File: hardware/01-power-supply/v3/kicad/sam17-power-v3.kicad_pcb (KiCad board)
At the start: 2 copper layers, 200 x 150 mm, 114 parts, among them J1 Barrier block 3 pos, J2 Molex KK-254 4 pos, J3 Barrier block 3 pos, J4 Barrier block 2 pos, J5 Faston macho 6.3mm PCB, J6 Molex KK-254 2 pos, J7 Barrier block 2 pos, J8 JST-PH 4 pos, U1 LM2941CT/NOPB, U10 ADS1115IDGSR — ADC 16 bits 4 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, U11 TMP1075DGKR — sensor de tempe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, U12 ISO1541D — aislador I2C bidir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, U2 LM2991T/NOPB, U3 LM7805, U4 LT3045EDD#TRPBF, U5 LT3045EDD#TRPBF, U6 LT3094EDD#PBF, U7 LT3094EDD#PBF, U8 INA226AIDGSR — monitor I/V I2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, U9 INA226AIDGSR — monitor I/V I2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

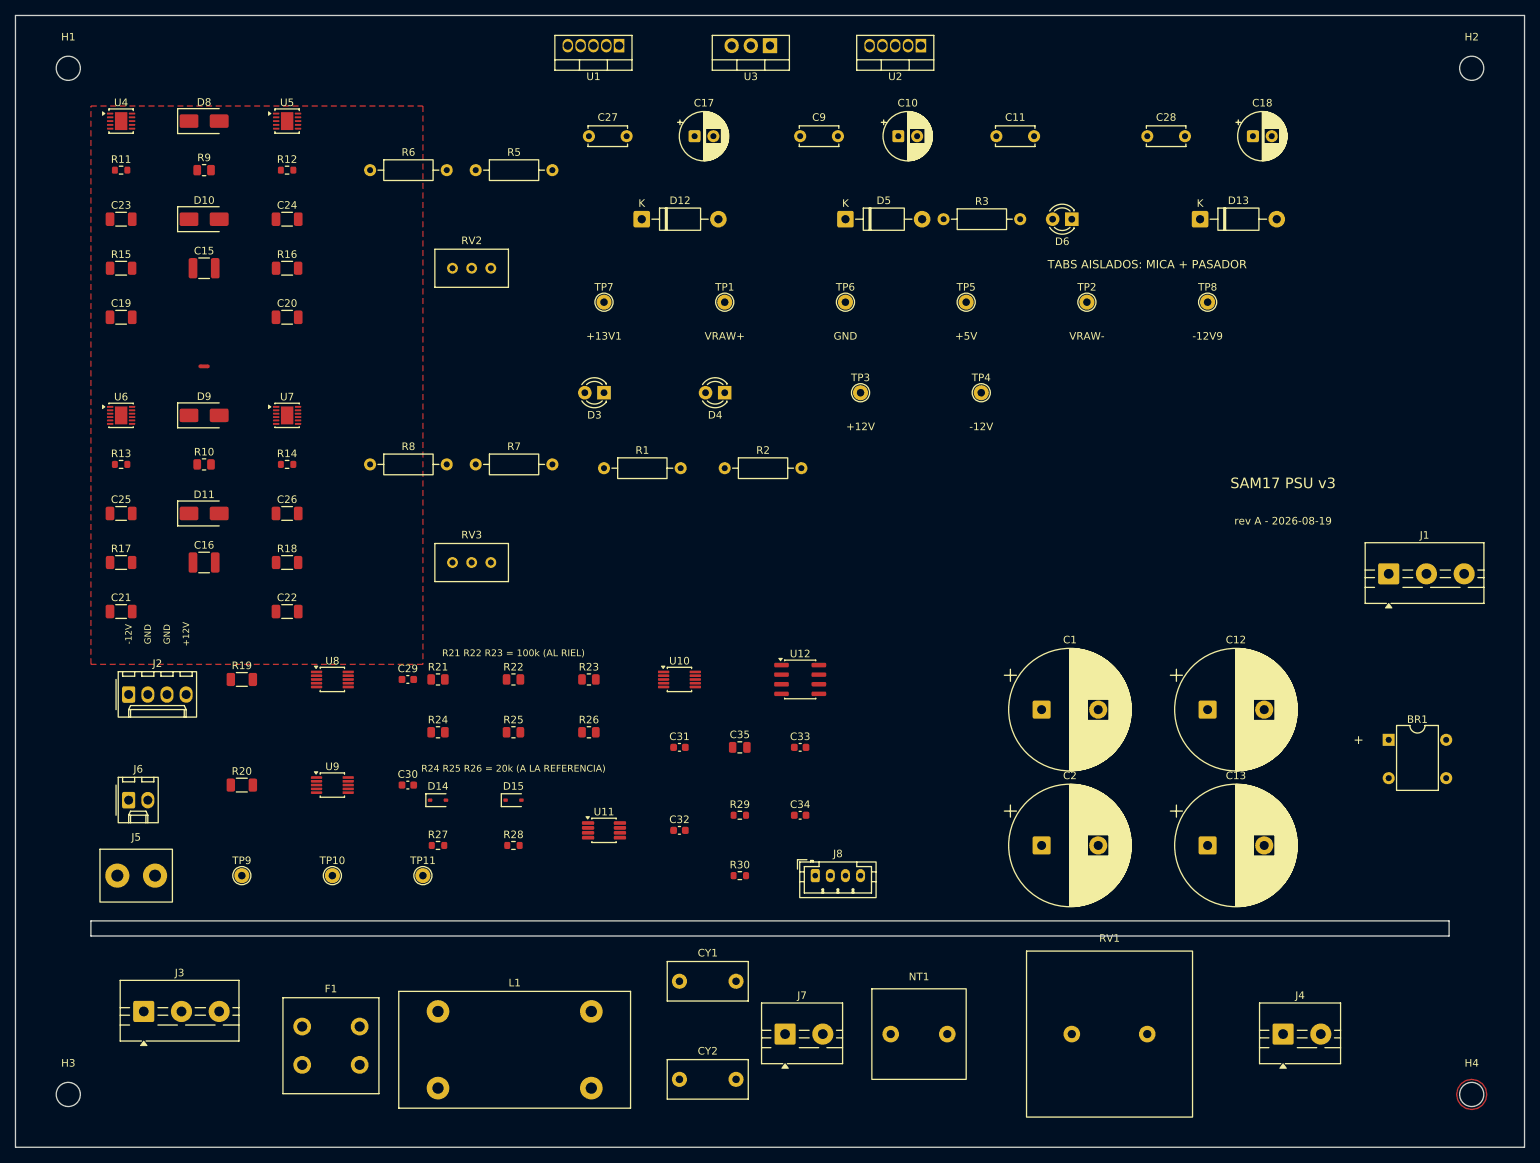
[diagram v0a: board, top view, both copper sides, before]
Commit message: Opcion B: GND entera en B.Cu como arbol, y la red repartida en carriles
81 de las 246 conexiones ruteadas, con las cuatro puertas de ruteo en cero:
0 cruces, 0 lazos en la masa, 0 pistas sobre pad ajeno, 0 vias contra nada.

GND — 68 pads, el 22% de la placa
--------------------------------
Un PEINE en B.Cu: tronco vertical en x=11 y siete costillas horizontales,
puestas en las bandas donde no hay ni un pad pasante (y = 11, 23, 44, 66, 84,
99, 117). Cada pad baja a su costilla por su propia x. Raiz electrica en J1.2,
la toma central del secundario, que es por donde vuelve la corriente de
rectificacion.

Va como arbol y no como plano porque un plano crea lazos, y un lazo alrededor
del puente rectificador es una espira de 100 Hz acoplada a todo lo demas. Las
costillas se parten en cada punto de enganche: si fueran un solo tramo de punta
a punta, el union-find de revisar_estrella() solo veria sus dos extremos y un
lazo de verdad pasaria sin que nadie lo viera.

Dos cosas salieron al hacerlo:

- Una via de 0.6 mm EN el pad de un chip de 0.5 mm de paso deja 0.03 mm al pin
  vecino. Lo midio revisar_vias() en 20 sitios. Ahora la via sale con un rabito
  corto en F.Cu hacia fuera del cuerpo, y se prueban las cuatro direcciones en
  orden -- porque "fuera del chip" no siempre es "libre": el rabito de C29
  esquivo a R21 yendose al oeste y aterrizo encima del OTRO pad de C29.
- El radio de busqueda empezo en 1.3 mm y la via de U9.7 no cabia por ningun
  lado. En un MSOP de 0.5 mm de paso, pedir 1.3 mm a los pines vecinos es pedir
  que el chip no exista. El numero real es 0.75: radio de la via mas aire.

LA RED — cinco carriles y un cruce que no se puede evitar colocando
------------------------------------------------------------------
El pinout del 8104-RC pone la entrada de L y la de N en esquinas OPUESTAS, asi
que sus salidas tambien: L_SMPS sale por abajo-izquierda y N_SMPS por
arriba-derecha, y las dos van al mismo sitio. Se cruzan se coloque el choke
donde se coloque.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
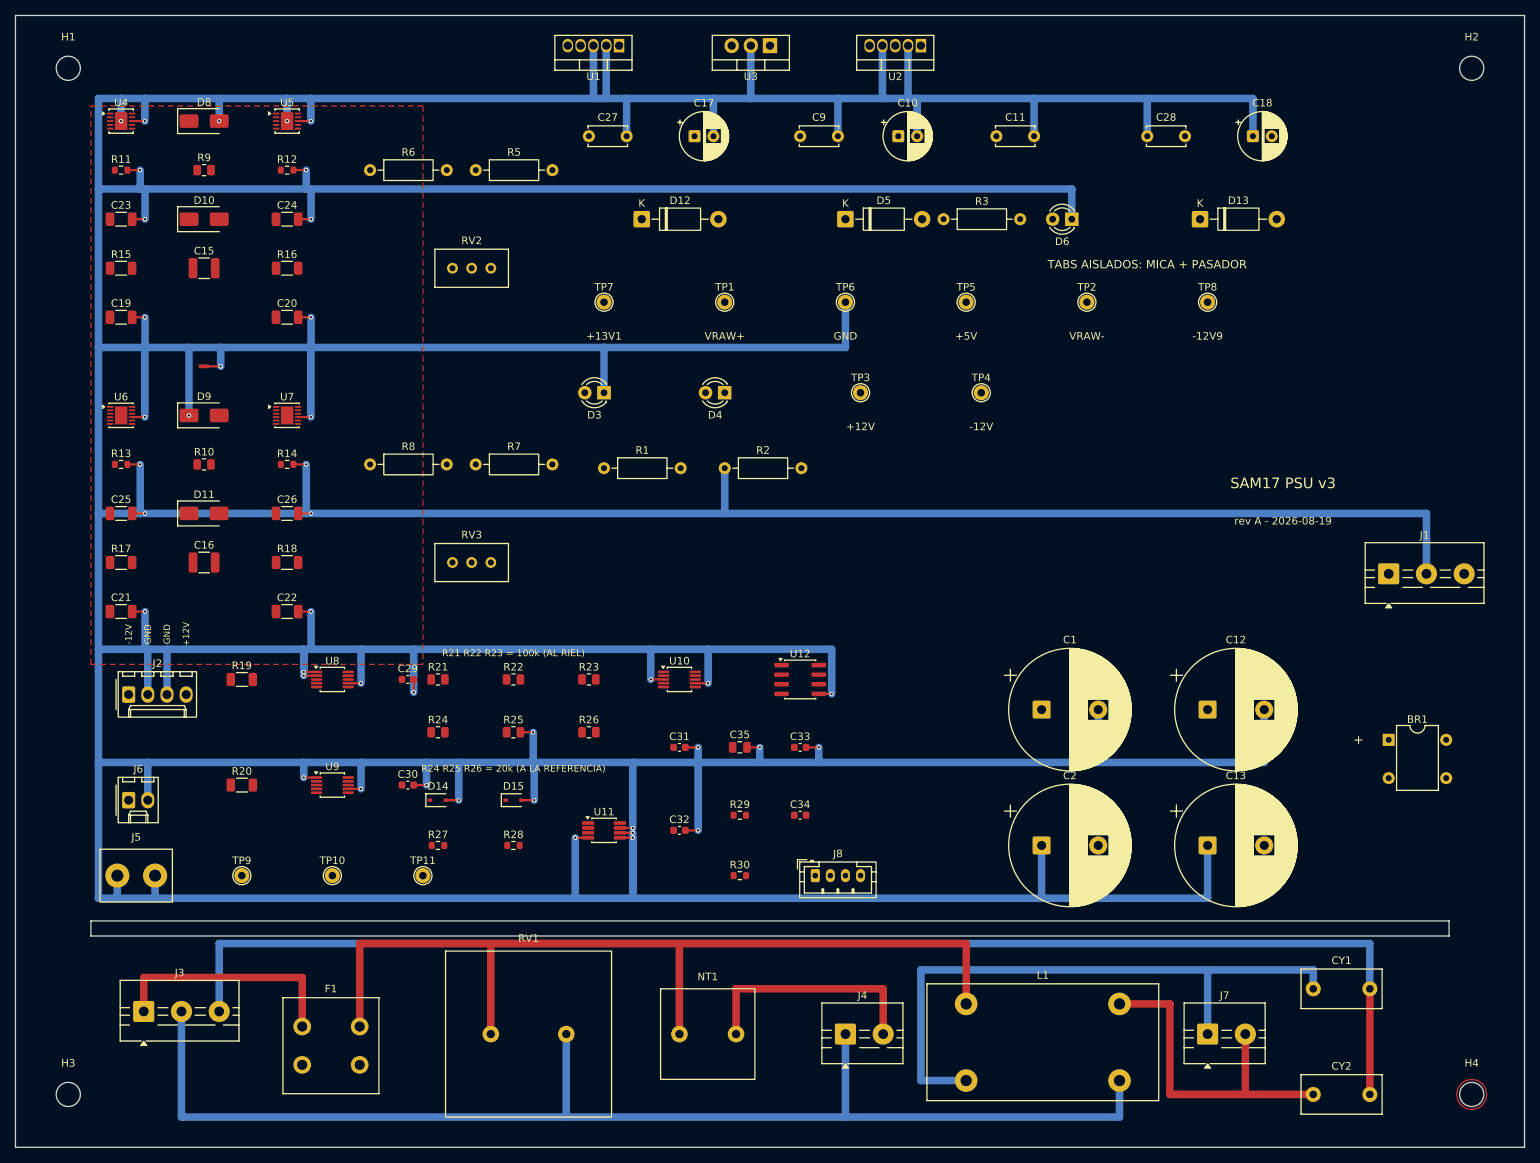
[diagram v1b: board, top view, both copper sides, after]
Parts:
- moved CY2 84.0 mm to (172.0, 143.0)
- moved CY1 84.0 mm to (172.0, 129.0)
- moved RV1 77.0 mm to (63.0, 135.0)
- moved L1 70.0 mm to (126.0, 131.0)
- moved J4 58.0 mm to (110.0, 135.0)
- moved J7 56.0 mm to (158.0, 135.0)
- moved NT1 28.0 mm to (88.0, 135.0)
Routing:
- net GND: track 0.00 -> 1468.2 mm, vias 0 -> 42
- net PE: track 0.00 -> 181.5 mm
- net /N: track 0.00 -> 165.2 mm
- net /L_F: track 0.00 -> 123.4 mm
- net /L_SMPS: track 0.00 -> 83.7 mm
- net /N_SMPS: track 0.00 -> 45.7 mm
- net /L: track 0.00 -> 32.0 mm
- net /L_TR: track 0.00 -> 31.5 mm

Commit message: Los cuatro rieles: la isla se entra por el norte y se sale por el este (#136)
120 de las 246 conexiones ruteadas (eran 81), con las cuatro puertas de ruteo
en cero: 0 cruces, 0 lazos, 0 pistas sobre pad ajeno, 0 vias contra nada.

LA ISLA ULTRA NO SE PUEDE CRUZAR. Es una rejilla SMD de 0.5 mm de paso, asi
que las pistas entran por los dos canales verticales que quedan libres entre
sus columnas -- x=9.5 al oeste de la columna 1, x=30.5 entre la 2 y la 3 -- y
solo se meten en horizontal en la y exacta de cada pad. Los dos canales sirven
a las dos mitades sin tocarse: entre la de +12 (y 13..40) y la de -12
(y 52..85) hay 8.4 mm de aire.

Y hay un sentido: +13V1 entra por el NORTE (carril y=11, entre la fila de
TO-220 y las columnas de soporte) y +12V sale por el ESTE (tronco x=43.5 hasta
el shunt). Entrar los dos por el mismo lado fue el primer intento y se cruzaban
en cuatro sitios.

CINCO BUCEOS DE DOS VIAS. El tronco de +12V separa la isla del resto en toda
la banda y 33..85, asi que lo que va de este a oeste tiene que pasarle por
debajo. Se hace donde el peine de masa deja hueco entre costillas -- 6 mm de
B.Cu entre la 44 y la 66, 16 mm entre la 66 y la 84 -- y se dice en el
comentario cual costilla se esta esquivando. No es un parche: en dos capas, un
cruce se paga en vias y lo unico que se elige es donde.

ESCAPAR UN DFN DE 0.5 mm CON PISTA DE 0.5 mm ES IMPOSIBLE. No queda aire ni al
pin de arriba ni al de abajo. ANCHO_ESCAPE = 0.2, y la pista se ensancha en
cuanto sale de debajo del chip.

LO QUE NO ESTA, Y NO ES DESCUIDO: las cuatro escapadas de OUTS. El pin OUTS de
un LT3045 es la realimentacion Kelvin; sale de un DFN de 0.5 mm de paso y su
vecino inmediato es el pin de GND, que ademas necesita su propia via. Una via
de 0.6 y una escapada de 0.2 a 0.5 mm de distancia no dejan los 0.127 de aire
que exige la fabricacion, se pongan como se pongan -- medido en las cuatro. Se
resuelven con la rejilla de la isla en la mano y es lo primero de la tanda que
viene, no u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
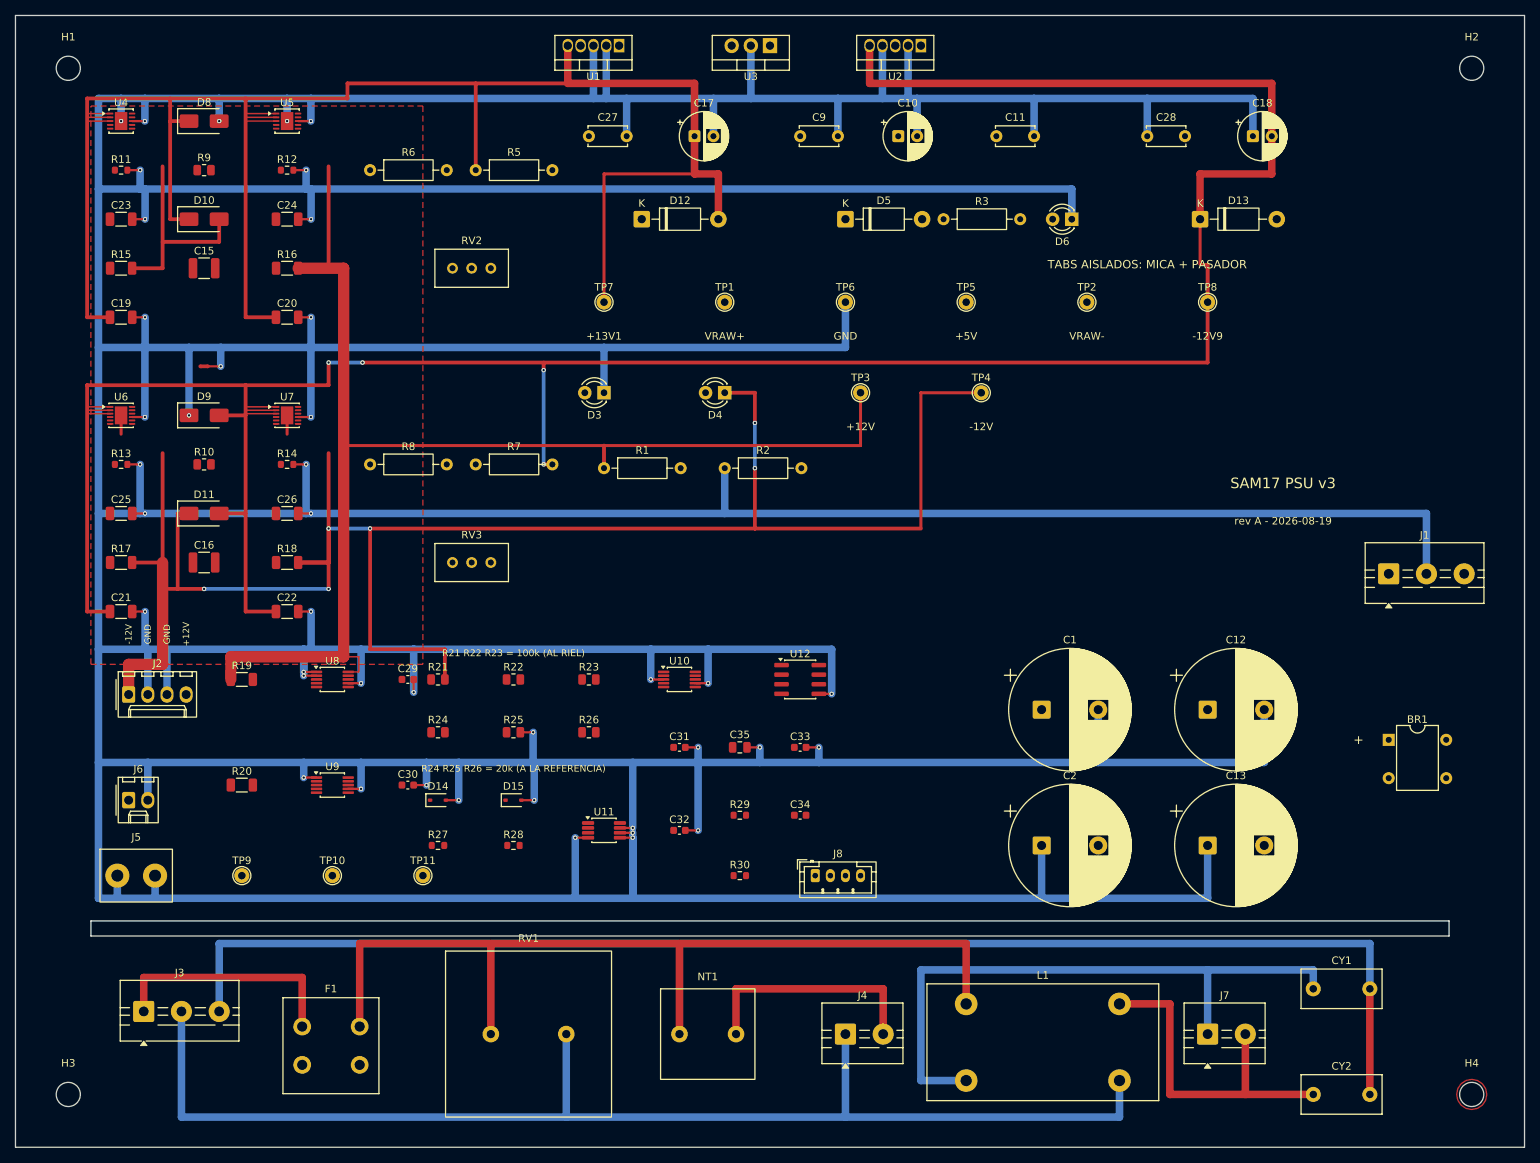
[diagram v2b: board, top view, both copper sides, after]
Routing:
- net /-12V9: track 0.00 -> 383.3 mm, vias 0 -> 4
- net -12V: track 0.00 -> 261.0 mm, vias 0 -> 6
- net /+13V1: track 0.00 -> 256.5 mm
- net +12V: track 0.00 -> 205.0 mm

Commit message: El ruteador estaba en el repo desde el modulo 2 y nadie lo habia importado
Fase C, Task 7. De 126 conexiones sin rutear a 11, y las 11 que quedan no
son del ruteo.

## Lo que se rutea a mano y lo que no

A mano va lo que se define por su FORMA: el arbol de GND (un plano crearia
una espira de 100 Hz alrededor del puente), los carriles de 230 V, los cuatro
rieles y el Kelvin de OUTS -- donde se suelda el sense de un LT3045 decide
que tension queda regulada. "El camino mas corto" es la respuesta equivocada
a esas preguntas.

El resto son 126 conexiones donde lo unico que se pide es no cruzarse con
nada, y para eso ya habia un BFS de Lee escrito, probado con su propia demo
y sin usar: `hardware/tools/maze.py`, escrito para el modulo 2. Ni la v1 ni
la v2 ni esta version lo habian importado nunca.

## Las cinco medidas que decidieron como se usa

* **Rejilla de 0.1 mm, no de 0.25.** Con 0.25 el riel de +5V dejo 5 pines al
  aire y los cinco eran el pin del MEDIO de un MSOP. Con 0.1, las 25
  conexiones de +5V en 25 s.
* **`via_ok` en O(1).** Preguntarle a `_hay_sitio()` -- que recorre los 310
  pads -- una vez por nodo no termino en diez minutos. La rejilla ya sabia
  responderlo: una clase de ancho mas, "via", y su mapa ES el mapa.
* **El clearance tenia TRES verdades y mandaba la que no estaba en el
  codigo.** `CLEARANCE_MM` = 0.127 y `m_MinClearance` = 0.127, pero el DRC
  compara contra la netclass del .kicad_pro, que estaba en el 0.2 de fabrica.
  34 infracciones de margen con las puertas propias en verde. `reglas()` no
  escribia ese fichero; ahora si.
* **El pasillo entre dos pines de 0.45 mm de paso mide 0.196 mm.** No admite
  margen de cortesia: `maze._pintar` redondeaba hacia fuera y se comia las
  dos unicas celdas, y sembrar un rabito de 0.3 mm como si fuera de 0.4
  (el calibre mas cercano por arriba) tapaba la que quedaba.
* **Una celda que reclaman dos redes no es de ninguna.** Se la quedaba la
  ultima en pintar y la otra la veia como propia: dos pistas 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
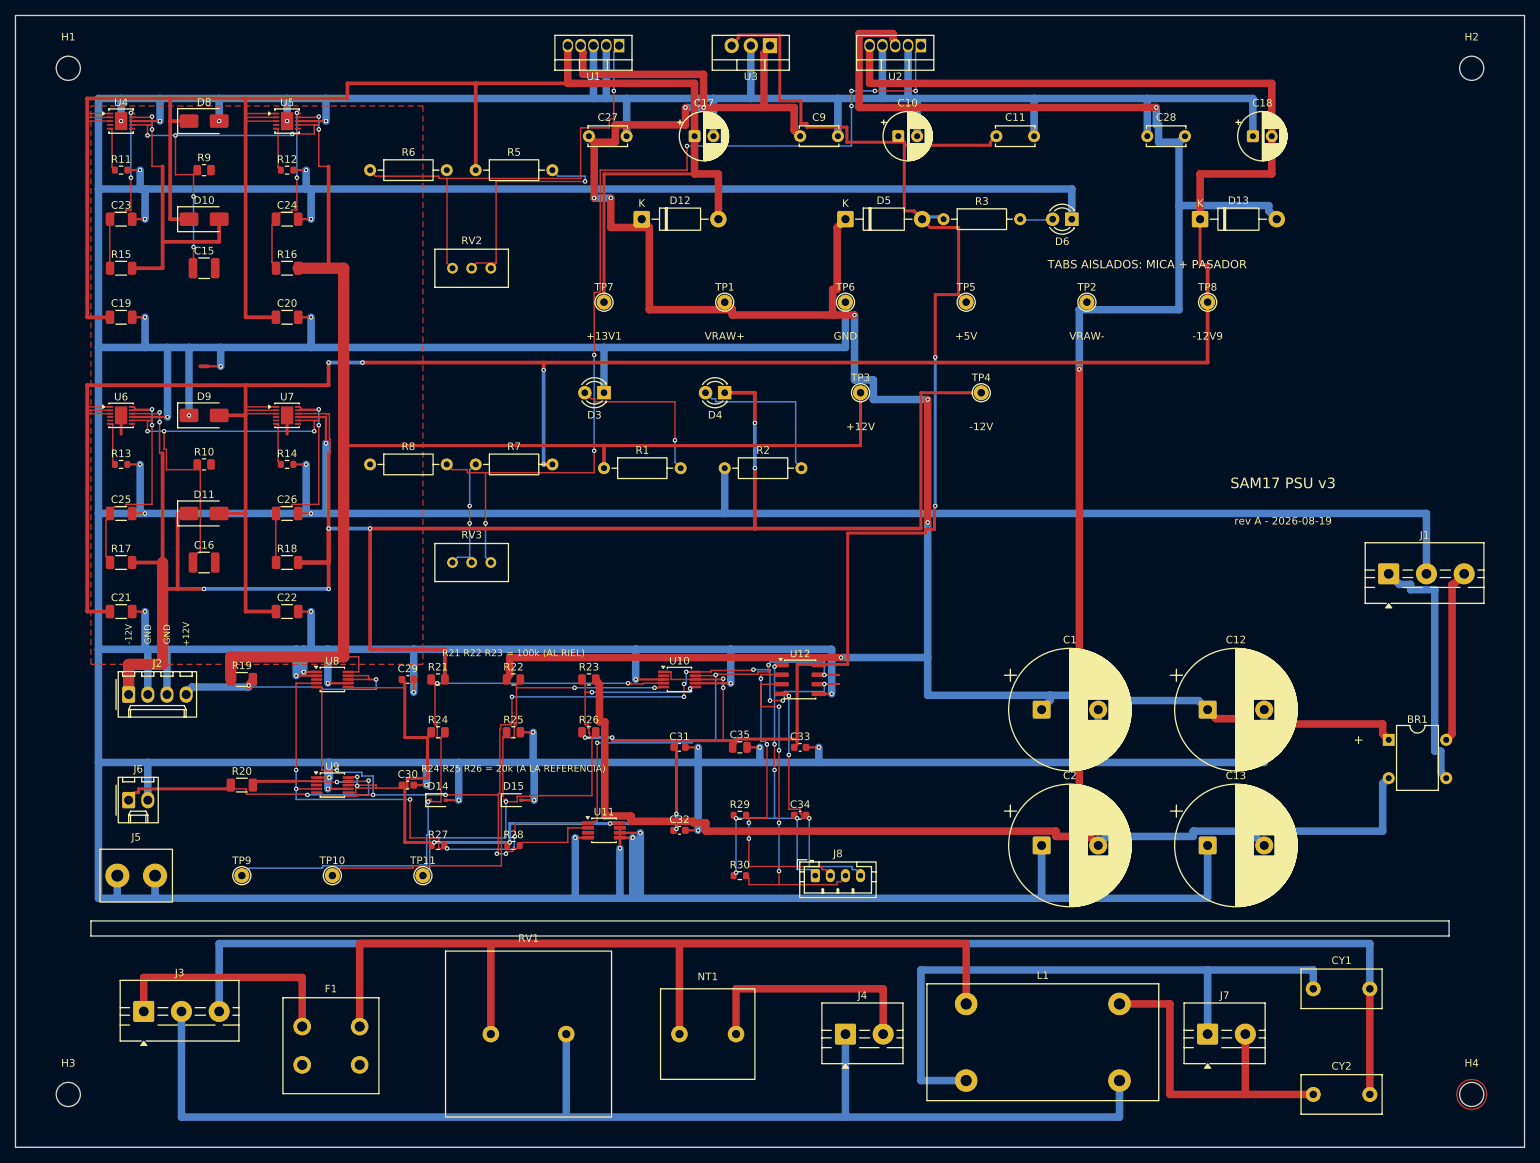
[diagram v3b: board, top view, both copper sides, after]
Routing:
- net +5V: track 0.00 -> 345.4 mm, vias 0 -> 14
- net /VRAW+: track 0.00 -> 333.0 mm, vias 0 -> 8
- net /VRAW-: track 0.00 -> 323.6 mm, vias 0 -> 2
- net /SCL_A: track 0.00 -> 141.7 mm, vias 0 -> 13
- net /SDA_A: track 0.00 -> 132.3 mm, vias 0 -> 9
- net Net-(U2-ADJ): track 0.00 -> 131.8 mm, vias 0 -> 8
- net /TAP_-12V: track 0.00 -> 86.7 mm, vias 0 -> 3
- net /TAP_VRAW+: track 0.00 -> 71.2 mm, vias 0 -> 2
- net /TAP_VRAW-: track 0.00 -> 66.2 mm, vias 0 -> 3
- net Net-(U1-ADJ): track 0.00 -> 63.0 mm, vias 0 -> 1
- net Net-(U6-SET): track 0.00 -> 56.0 mm, vias 0 -> 3
- net Net-(U4-SET): track 0.00 -> 53.1 mm, vias 0 -> 5
- net +3V3: track 0.00 -> 48.6 mm, vias 0 -> 6
- net /SCL_D: track 0.00 -> 46.7 mm, vias 0 -> 4
- net /SDA_D: track 0.00 -> 44.0 mm, vias 0 -> 4
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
